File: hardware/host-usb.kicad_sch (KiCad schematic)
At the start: 24 parts, among them IC10 DSC6101CI2A-024.0000, IC8 I2C-EEPROM, IC9 CY7C68013A-56PVXC

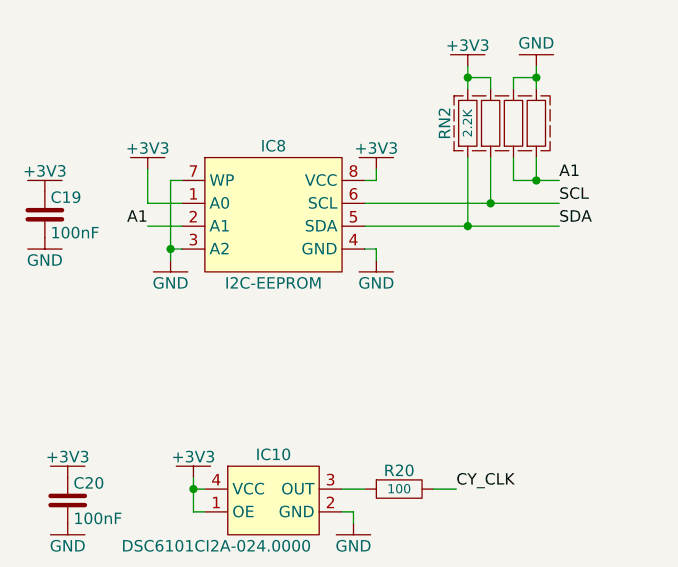
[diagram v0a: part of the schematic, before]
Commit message: Added EEPROM part name
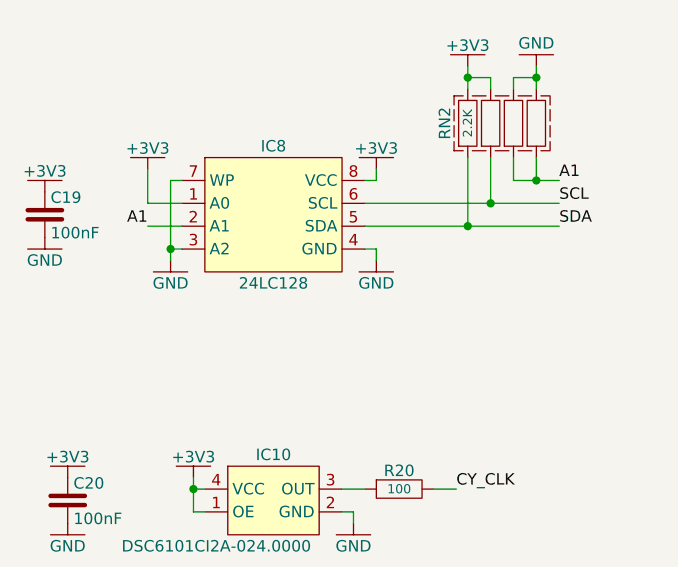
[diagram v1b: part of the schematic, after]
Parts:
- IC8: value I2C-EEPROM -> 24LC128
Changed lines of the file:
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@@
   (paper "USLetter")
   (title_block
-    (date "2023-05-06")
+    (date "2023-06-16")
     (rev "6")
   )
@@
       (effects (font (size 1.27 1.27)))
     )
-    (property "Value" "I2C-EEPROM" (at 81.28 68.58 0)
+    (property "Value" "24LC128" (at 81.28 68.58 0)
       (effects (font (size 1.27 1.27)))
     )
